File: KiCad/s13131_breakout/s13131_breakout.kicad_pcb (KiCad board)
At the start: 2 copper layers, 33 x 20.4 mm, 5 parts, among them J1 Conn_01x07_Pin

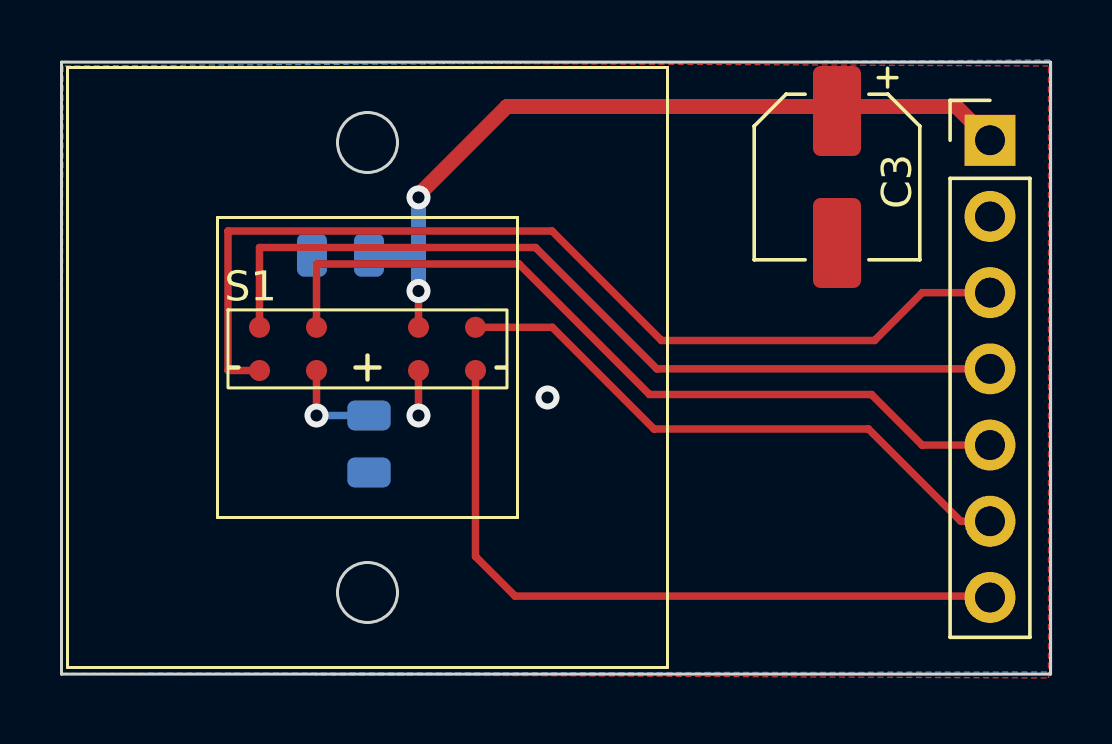
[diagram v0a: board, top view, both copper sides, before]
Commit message: Updated breakout board and schematic.
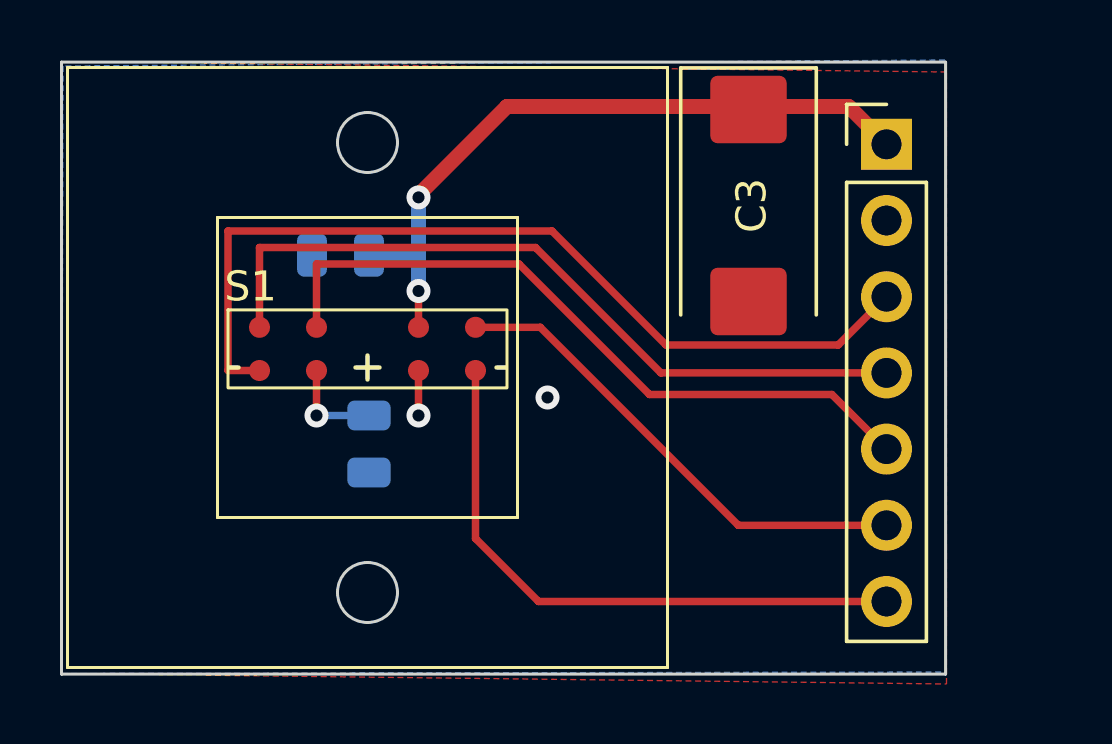
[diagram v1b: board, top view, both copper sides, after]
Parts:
- C3: footprint Capacitor_SMD:CP_Elec_5x5.4 -> Capacitor_Tantalum_SMD:CP_EIA-7343-15_Kemet-W_Pad2.25x2.55mm_HandSolder
- moved J1 3.45 mm to (63.3, 51.1)
- moved C3 3.10 mm to (58.7, 53.1)
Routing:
- net /Video: track 23.9 -> 20.2 mm
- net +3.3V: track 27.0 -> 23.5 mm
- net /ST: track 28.7 -> 25.3 mm
- net /EOS: track 19.8 -> 16.4 mm
- net /Trig: track 27.1 -> 23.7 mm
- net /CLK: track 33.3 -> 29.9 mm
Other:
- board size 33 x 20.4 mm -> 29.5 x 20.4 mm

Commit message: Sent breakout v0.1 to production.
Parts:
- C3: moved to B.Cu
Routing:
- net /ST: track 25.3 -> 26.0 mm
- net +3.3V: track 23.5 -> 23.6 mm, vias 2 -> 1
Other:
- board size 29.5 x 20.4 mm -> 30 x 20.4 mm
- board text added: "CLK"
- board text added: "EOS"
- board text added: "GND"
- board text added: "ST"
- board text added: "Trig"
- board text added: "VCC"
- board text added: "Video"
- board text added: "s13131"
- board text added: "v0.1"
- board text added: "ॐ"
